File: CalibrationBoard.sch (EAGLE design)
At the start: 113 parts, among them J1 BANANA_CONN, J2 BANANA_CONN, J3 BANANA_CONN, J4 BANANA_CONN, J5 BANANA_CONN, J6 BANANA_CONN, J7 BANANA_CONN, J8 BANANA_CONN, J9 BANANA_CONN, Q1 IRF540, U1 MAX6126AASA25+, U2 MAX6126AASA25+, U3 MAX6126AASA50+

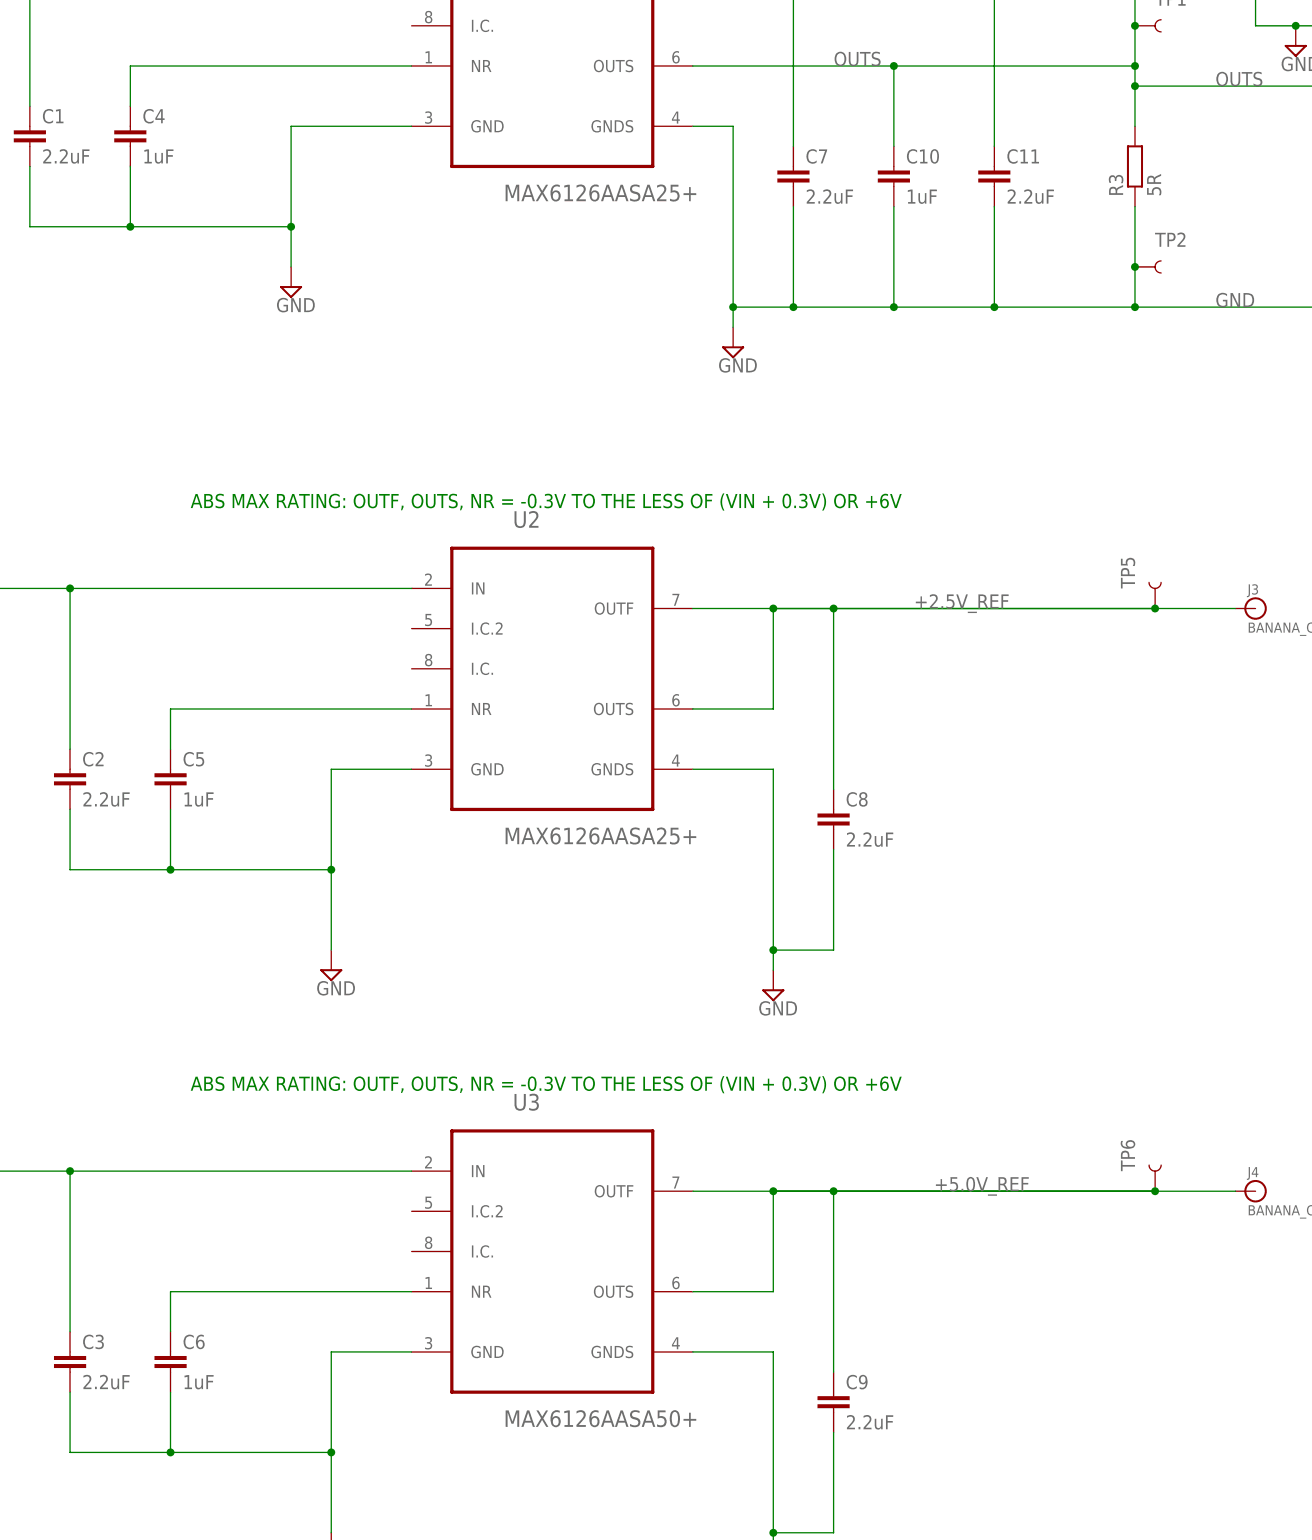
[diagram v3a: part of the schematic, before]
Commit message: Various minor changes with minor CAD impacts
Connected some minor air nets (no CAD issues)
Changed NR caps from 1uF to 0.1uF as per DS.
Moved a decoupling cap to allow ground flood to IC.
Standardised the plane to track separation.
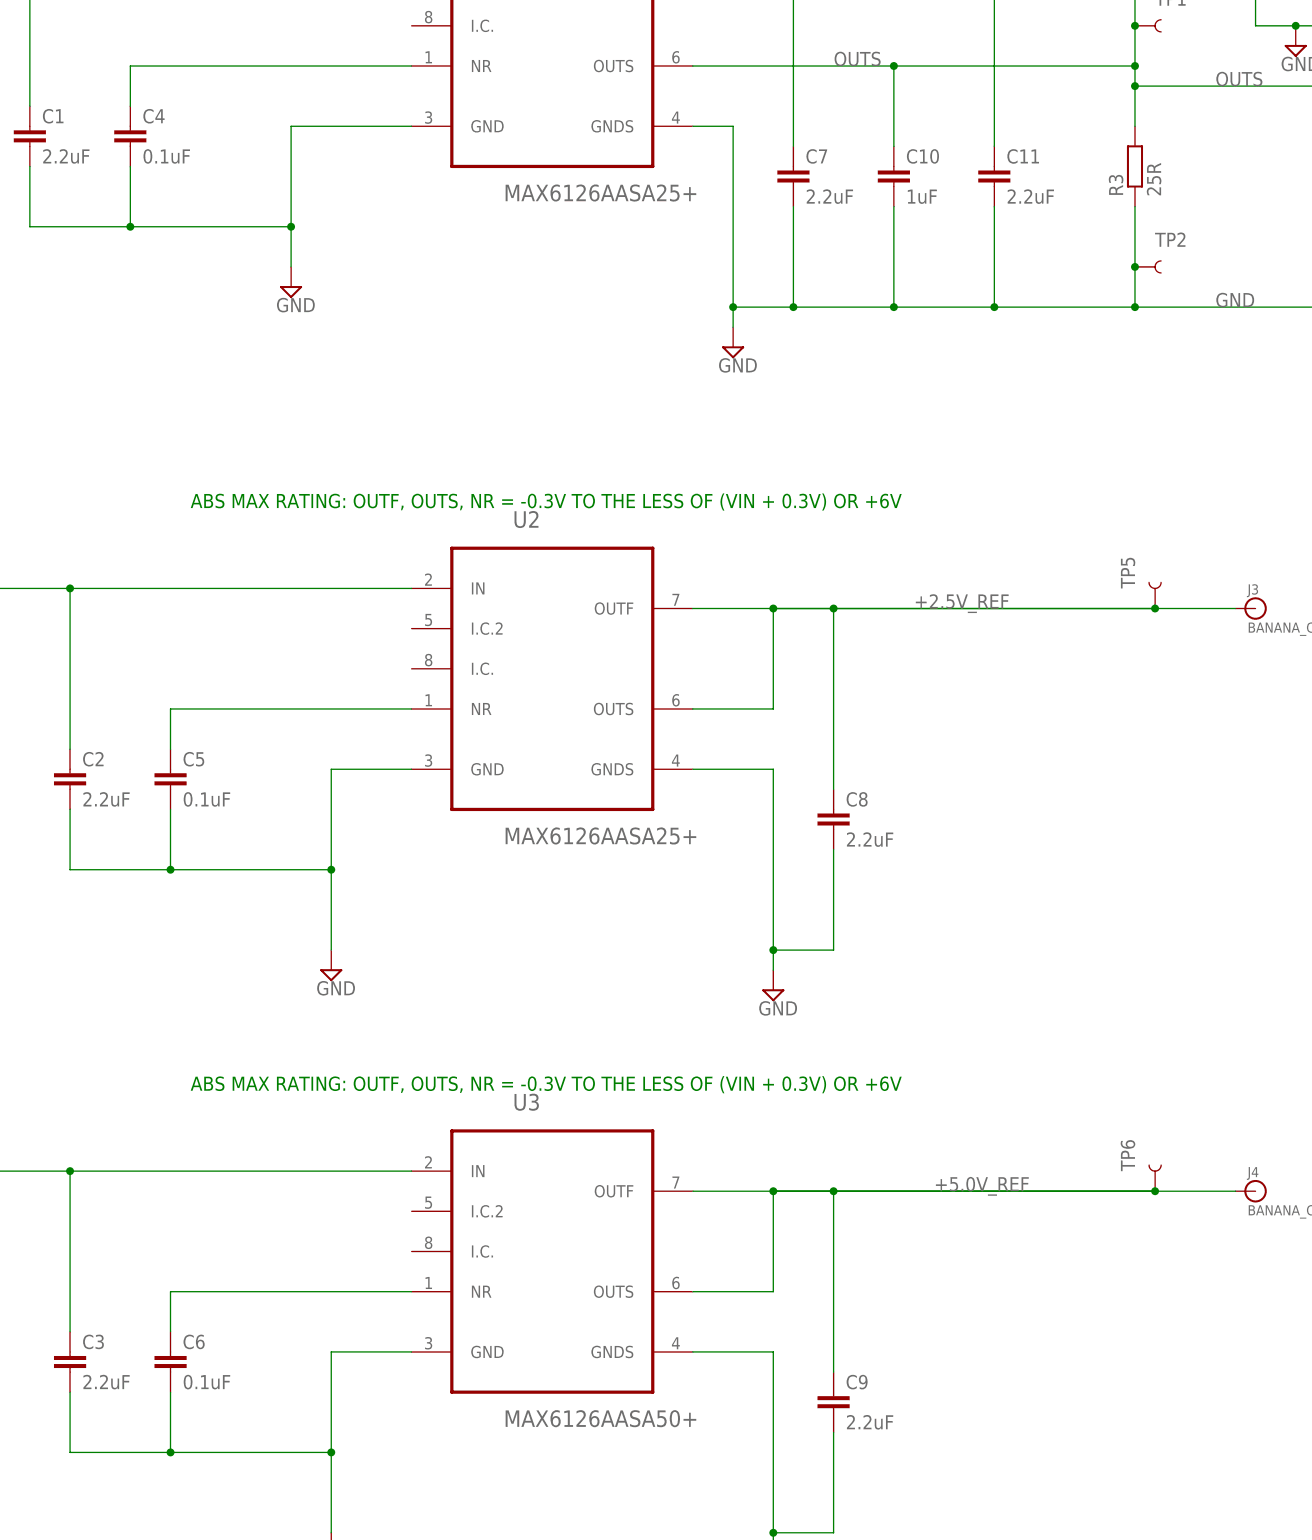
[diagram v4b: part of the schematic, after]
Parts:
- C4, C5, C6: value 1uF -> 0.1uF
- R3: value 5R -> 25R
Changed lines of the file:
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@@
 <grid distance="0.1" unitdist="inch" unit="inch" style="lines" multiple="1" display="no" altdistance="0.01" altunitdist="inch" altunit="inch"/>
 <layers>
-<layer number="1" name="Top" color="4" fill="1" visible="yes" active="no"/>
-<layer number="16" name="Bottom" color="1" fill="1" visible="yes" active="no"/>
-<layer number="17" name="Pads" color="2" fill="1" visible="yes" active="no"/>
-<layer number="18" name="Vias" color="2" fill="1" visible="yes" active="no"/>
-<layer number="19" name="Unrouted" color="6" fill="1" visible="yes" active="no"/>
-<layer number="20" name="Dimension" color="15" fill="1" visible="yes" active="no"/>
-<layer number="21" name="tPlace" color="7" fill="1" visible="yes" active="no"/>
-<layer number="22" name="bPlace" color="7" fill="1" visible="yes" active="no"/>
-<layer number="23" name="tOrigins" color="15" fill="1" visible="yes" active="no"/>
-<layer number="24" name="bOrigins" color="15" fill="1" visible="yes" active="no"/>
-<layer number="25" name="tNames" color="7" fill="1" visible="yes" active="no"/>
-<layer number="26" name="bNames" color="7" fill="1" visible="yes" active="no"/>
-<layer number="27" name="tValues" color="7" fill="1" visible="yes" active="no"/>
-<layer number="28" name="bValues" color="7" fill="1" visible="yes" active="no"/>
+<layer number="1" name="Top" color="4" fill="1" visible="no" active="no"/>
+<layer number="16" name="Bottom" color="1" fill="1" visible="no" active="no"/>
+<layer number="17" name="Pads" color="2" fill="1" visible="no" active="no"/>
+<layer number="18" name="Vias" color="2" fill="1" visible="no" active="no"/>
+<layer number="19" name="Unrouted" color="6" fill="1" visible="no" active="no"/>
+<layer number="20" name="Dimension" color="15" fill="1" visible="no" active="no"/>
+<layer number="21" name="tPlace" color="7" fill="1" visible="no" active="no"/>
+<layer number="22" name="bPlace" color="7" fill="1" visible="no" active="no"/>
+<layer number="23" name="tOrigins" color="15" fill="1" visible="no" active="no"/>
+<layer number="24" name="bOrigins" color="15" fill="1" visible="no" active="no"/>
+<layer number="25" name="tNames" color="7" fill="1" visible="no" active="no"/>
+<layer number="26" name="bNames" color="7" fill="1" visible="no" active="no"/>
+<layer number="27" name="tValues" color="7" fill="1" visible="no" active="no"/>
+<layer number="28" name="bValues" color="7" fill="1" visible="no" active="no"/>
 <layer number="29" name="tStop" color="7" fill="3" visible="no" active="no"/>
 <layer number="30" name="bStop" color="7" fill="6" visible="no" active="no"/>
@@
 <layer number="35" name="tGlue" color="7" fill="4" visible="no" active="no"/>
 <layer number="36" name="bGlue" color="7" fill="5" visible="no" active="no"/>
-<layer number="37" name="tTest" color="7" fill="1" visible="yes" active="no"/>
-<layer number="38" name="bTest" color="7" fill="1" visible="yes" active="no"/>
+<layer number="37" name="tTest" color="7" fill="1" visible="no" active="no"/>
+<layer number="38" name="bTest" color="7" fill="1" visible="no" active="no"/>
 <layer number="39" name="tKeepout" color="4" fill="11" visible="no" active="no"/>
 <layer number="40" name="bKeepout" color="1" fill="11" visible="no" active="no"/>
@@
 <layer number="44" name="Drills" color="7" fill="1" visible="no" active="no"/>
 <layer number="45" name="Holes" color="7" fill="1" visible="no" active="no"/>
-<layer number="46" name="Milling" color="3" fill="1" visible="yes" active="no"/>
-<layer number="47" name="Measures" color="7" fill="1" visible="yes" active="no"/>
-<layer number="48" name="Document" color="7" fill="1" visible="yes" active="no"/>
-<layer number="49" name="Reference" color="7" fill="1" visible="yes" active="no"/>
-<layer number="50" name="dxf" color="7" fill="1" visible="yes" active="no"/>
-<layer number="51" name="tDocu" color="7" fill="1" visible="yes" active="no"/>
-<layer number="52" name="bDocu" color="7" fill="1" visible="yes" active="no"/>
-<layer number="53" name="tGND_GNDA" color="7" fill="9" visible="yes" active="no"/>
-<layer number="54" name="bGND_GNDA" color="1" fill="9" visible="yes" active="no"/>
-<layer number="56" name="wert" color="7" fill="1" visible="yes" active="no"/>
-<layer number="57" name="tCAD" color="7" fill="1" visible="yes" active="no"/>
+<layer number="46" name="Milling" color="3" fill="1" visible="no" active="no"/>
+<layer number="47" name="Measures" color="7" fill="1" visible="no" active="no"/>
+<layer number="48" name="Document" color="7" fill="1" visible="no" active="no"/>
+<layer number="49" name="Reference" color="7" fill="1" visible="no" active="no"/>
+<layer number="50" name="dxf" color="7" fill="1" visible="no" active="no"/>
+<layer number="51" name="tDocu" color="7" fill="1" visible="no" active="no"/>
+<layer number="52" name="bDocu" color="7" fill="1" visible="no" active="no"/>
+<layer number="53" name="tGND_GNDA" color="7" fill="9" visible="no" active="no"/>
+<layer number="54" name="bGND_GNDA" color="1" fill="9" visible="no" active="no"/>
+<layer number="56" name="wert" color="7" fill="1" visible="no" active="no"/>
+<layer number="57" name="tCAD" color="7" fill="1" visible="no" active="no"/>
 <layer number="90" name="Modules" color="5" fill="1" visible="yes" active="yes"/>
 <layer number="91" name="Nets" color="2" fill="1" visible="yes" active="yes"/>
@@
 <attribute name="OC_FARNELL" value="unknown"/>
 </part>
-<part name="C4" library="rcl" deviceset="C-EU" device="C0805" value="1uF">
+<part name="C4" library="rcl" deviceset="C-EU" device="C0805" value="0.1uF">
 <attribute name="MF" value=""/>
 <attribute name="MPN" value=""/>
@@
 <attribute name="OC_FARNELL" value="unknown"/>
 </part>
-<part name="R3" library="rcl" deviceset="R-EU_" device="R0805" value="5R">
+<part name="R3" library="rcl" deviceset="R-EU_" device="R0805" value="25R">
 <attribute name="MF" value=""/>
 <attribute name="MPN" value=""/>
@@
 <attribute name="OC_FARNELL" value="unknown"/>
 </part>
-<part name="C5" library="rcl" deviceset="C-EU" device="C0805" value="1uF">
+<part name="C5" library="rcl" deviceset="C-EU" device="C0805" value="0.1uF">
 <attribute name="MF" value=""/>
 <attribute name="MPN" value=""/>
@@
 <attribute name="OC_FARNELL" value="unknown"/>
 </part>
-<part name="C6" library="rcl" deviceset="C-EU" device="C0805" value="1uF">
-<attribute name="MF" value=""/>
-<attribute name="MPN" value=""/>
+<part name="C6" library="rcl" deviceset="C-EU" device="C0805" value="0.1uF">
+<attribute name="MF" value=""/>
+<attribute name="MPN" value=""/>

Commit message: latest commits
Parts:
- BAT1: value +9V_BATTERY -> +9V_BATTERY_HOLDER
- C12: value 10pF -> 47pF; MF (none) -> AVX; MPN (none) -> 08052U470FAT2A; OC_FARNELL unknown -> 2332727
- C13: value 1nF -> 1.2nF; MF (none) -> VISHAY VITRAMON; MPN (none) -> VJ0805A122FXBMT; OC_FARNELL unknown -> 1650948
- C15: MF (none) -> AVX; MPN (none) -> 08055C104JAT2A; OC_FARNELL unknown -> 1740673
- J1, J3, J4, J5, J7: value BANANA_CONN -> BANANA_CONN_RED; MF (none) -> HIRSCHMANN TEST AND MEASUREMENT; MPN (none) -> 972354101; OC_FARNELL unknown -> 1011402
- J2, J6, J8, J9: value BANANA_CONN -> BANANA_CONN_BLACK; MF (none) -> HIRSCHMANN TEST AND MEASUREMENT; MPN (none) -> 972354101; OC_FARNELL unknown -> 1011402
- L3: MPN 0603AF-102XJRU -> 1812PS-102JLC; OC_FARNELL 2285913RL -> 2287053
- L5: value 10mH -> 4.7mH; MF (none) -> WURTH ELEKTRONIK; MPN (none) -> 7447721047; OC_FARNELL unknown -> 2211696
- LED1: value GREEN_LED -> RED_LED; MF (none) -> DIALIGHT; MPN (none) -> 597-3121-207F; OC_FARNELL unknown -> 1519491
- Q1: value IRF540 -> IRF3708PBF; MF MULTICOMP -> INTERNATIONAL RECTIFIER; MPN SR16150 -> IRF3708PBF; OC_FARNELL 1625239 -> 8648158
- R10: MF (none) -> PANASONIC ELECTRONIC COMPONENTS; MPN (none) -> ERA6AEB102V; OC_FARNELL unknown -> 1577659
- R12: MF (none) -> SUSUMU; MPN (none) -> RR1220P-103-B-T5; OC_FARNELL unknown -> 1653282
- R13: MF (none) -> SUSUMU; MPN (none) -> RR1220P-104-B-T5; OC_FARNELL unknown -> 1653285
- R14: MF (none) -> SUSUMU; MPN (none) -> RR1220P-105-B-T5; OC_FARNELL unknown -> 1653287
- R4: MF (none) -> PANASONIC ELECTRONIC COMPONENTS; MPN (none) -> ERJ6RSFR10V; OC_FARNELL unknown -> 1717785
- R5: MF (none) -> BOURNS; MPN (none) -> CR0805-FX-1R00ELF; OC_FARNELL unknown -> 2333617
- R7: MF COILCRAFT -> BOURNS; MPN 1008LS-393XJLB -> CRT0805-BY-10R0ELF; OC_FARNELL 2286860 -> 2008313
- R9: MF (none) -> SUSUMU; MPN (none) -> RR1220P-101-B-T5; OC_FARNELL unknown -> 1653279
- TP1, TP10, TP11, TP12, TP13, TP14, TP15, TP16, TP17, TP18, TP19, TP2, TP20, TP21, TP22, TP23, TP24, TP25, TP26, TP27, TP28, TP29, TP3, TP30, TP31, TP32, TP33, TP34, TP35, TP36, TP37, TP38, TP39, TP4, TP40, TP41, TP42, TP43, TP44, TP45, TP46, TP47, TP48, TP49, TP5, TP6, TP7, TP8, TP9: MF (none) -> MULTICOMP; MPN (none) -> TEST-3; OC_FARNELL unknown -> 1702006
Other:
- note added: "5.6V to 12.6V"
- note added: "Current measurement MAX6126 needs to be a 4.0v or less due to max rating in the OUTF line. This assumes Vgs(th) of <= 2.0v."
- note removed: "FIX THE CAPS AND INDUCTORS, CHECK THE SEPARATION OF THE TEST POINTS FOR THE TWEEZERS"
- note removed: "MAX6126 needs to be a 4.0v or less due to max rating in the OUTF line"
- moved on the sheet: BAT1, F1, F2, J9, KK1, PAD1, PAD2, PAD3, PAD4, PAD5, PAD6, TP7

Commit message: latest updates
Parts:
- removed J9: BANANA_CONN_BLACK, SparkFun-Connectors:BANANA_CONN
- removed PAD1, PAD2, PAD3, PAD4, PAD5, PAD6: MOUNT_HOLE, wirepad:3,81/1,4
- added C19: 100uF, rcl:CPOL-USE5-10.5
- added H1, H2, H3, H4: MOUNT-PAD-ROUND3.3, holes:MOUNT-PAD-ROUND3.3
- F1: device fuse:FUSELITTLEFUSE -> RGEF1200:RGEF1200; MPN RGEF1200 -> (none); OC_FARNELL 1345957 -> (none)
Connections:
- net GND: now also C19.-, H1.MOUNT, H2.MOUNT, H3.MOUNT, H4.MOUNT; no longer J9.1, PAD1.P, PAD2.P, PAD3.P, PAD4.P, PAD5.P, PAD6.P
- net V_IN_2: now also C19.+
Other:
- moved on the sheet: D1, TP7
